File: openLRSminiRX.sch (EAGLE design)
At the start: 32 parts, among them IC1 MCP1703CB, U1 ATMEGA328P, Y1 16MHz

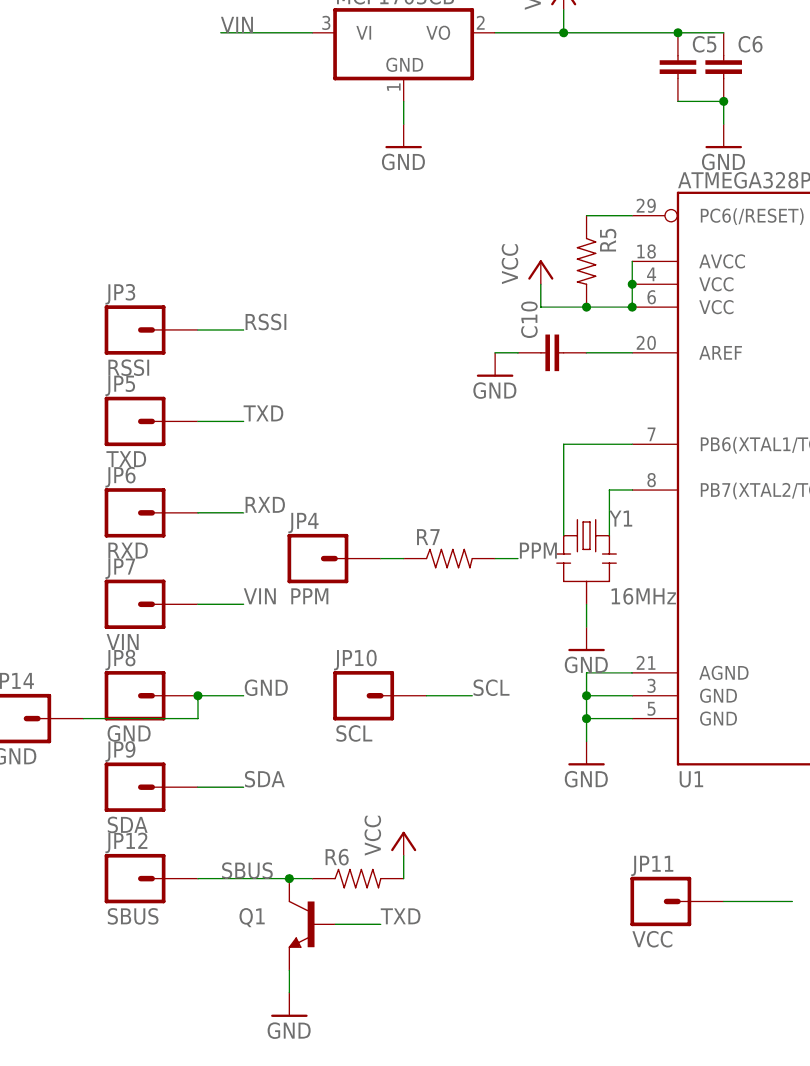
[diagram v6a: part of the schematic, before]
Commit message: Fix SBUS inverter (add resistor between TXD and NPN B) Add DTR breakout (easier serial flashing)
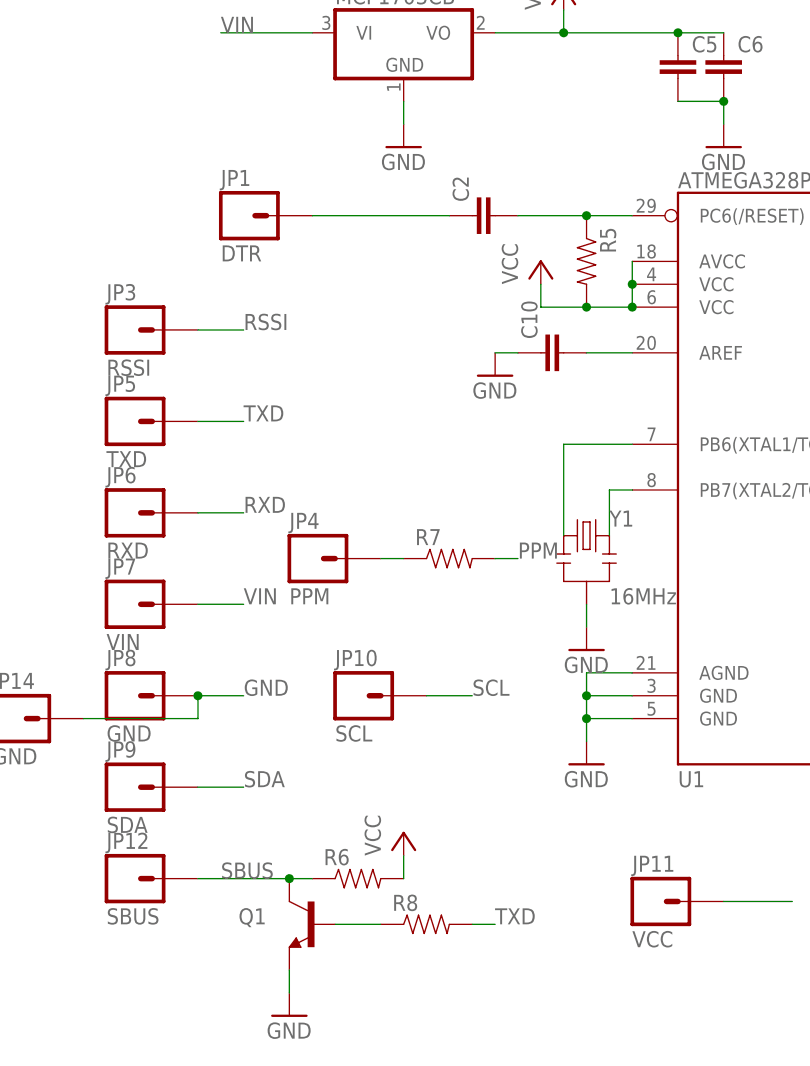
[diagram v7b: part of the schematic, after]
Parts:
- added C2: (no value), SparkFun-Capacitors:CAP0805
- added JP1: DTR, SparkFun-Connectors:M01PTH
- added R8: (no value), SparkFun-Resistors:RESISTOR0805-RES
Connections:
- new net N$20: C2.1, JP1.1
- new net N$21: Q1.B, R8.1
- net N$18: now also C2.2
- net TXD: now also R8.2; no longer Q1.B
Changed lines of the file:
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@@
 <?xml version="1.0" encoding="utf-8"?>
 <!DOCTYPE eagle SYSTEM "eagle.dtd">
-<eagle version="6.4">
+<eagle version="7.1.0">
 <drawing>
 <settings>
@@
 <part name="Y1" library="SparkFun-FreqCtrl" deviceset="RESONATOR" device="16MHZ" value="16MHz"/>
 <part name="GND12" library="supply1" deviceset="GND" device=""/>
+<part name="JP1" library="SparkFun-Connectors" deviceset="M01" device="PTH" value="DTR"/>
+<part name="C2" library="SparkFun-Capacitors" deviceset="CAP" device="0805"/>
+<part name="R8" library="SparkFun-Resistors" deviceset="RESISTOR" device="0805-RES"/>
 </parts>
 <sheets>
@@
 <instance part="Y1" gate="G$1" x="22.86" y="50.8"/>
 <instance part="GND12" gate="1" x="22.86" y="38.1"/>
+<instance part="JP1" gate="G$1" x="-15.24" y="86.36"/>
+<instance part="C2" gate="G$1" x="12.7" y="86.36" rot="R90"/>
+<instance part="R8" gate="G$1" x="5.08" y="7.62"/>
 </instances>
 <busses>
@@
 </segment>
 <segment>
-<pinref part="Q1" gate="G$1" pin="B"/>
-<wire x1="-5.08" y1="7.62" x2="0" y2="7.62" width="0.1524" layer="91"/>
-<label x="0" y="7.62" size="1.778" layer="95"/>
+<pinref part="R8" gate="G$1" pin="2"/>
+<wire x1="10.16" y1="7.62" x2="12.7" y2="7.62" width="0.1524" layer="91"/>
+<label x="12.7" y="7.62" size="1.778" layer="95"/>
 </segment>
 </net>
@@
 <pinref part="U1" gate="G$1" pin="PC6(/RESET)"/>
 <wire x1="22.86" y1="86.36" x2="27.94" y2="86.36" width="0.1524" layer="91"/>
+<pinref part="C2" gate="G$1" pin="2"/>
+<wire x1="22.86" y1="86.36" x2="15.24" y2="86.36" width="0.1524" layer="91"/>
+<junction x="22.86" y="86.36"/>
 </segment>
 </net>
@@
 </segment>
 </net>
+<net name="N$20" class="0">
+<segment>
+<pinref part="JP1" gate="G$1" pin="1"/>
+<pinref part="C2" gate="G$1" pin="1"/>
+<wire x1="-7.62" y1="86.36" x2="7.62" y2="86.36" width="0.1524" layer="91"/>
+</segment>
+</net>
+<net name="N$21" class="0">
+<segment>
+<pinref part="R8" gate="G$1" pin="1"/>
+<pinref part="Q1" gate="G$1" pin="B"/>
+<wire x1="0" y1="7.62" x2="-5.08" y2="7.62" width="0.1524" layer="91"/>
+</segment>
+</net>

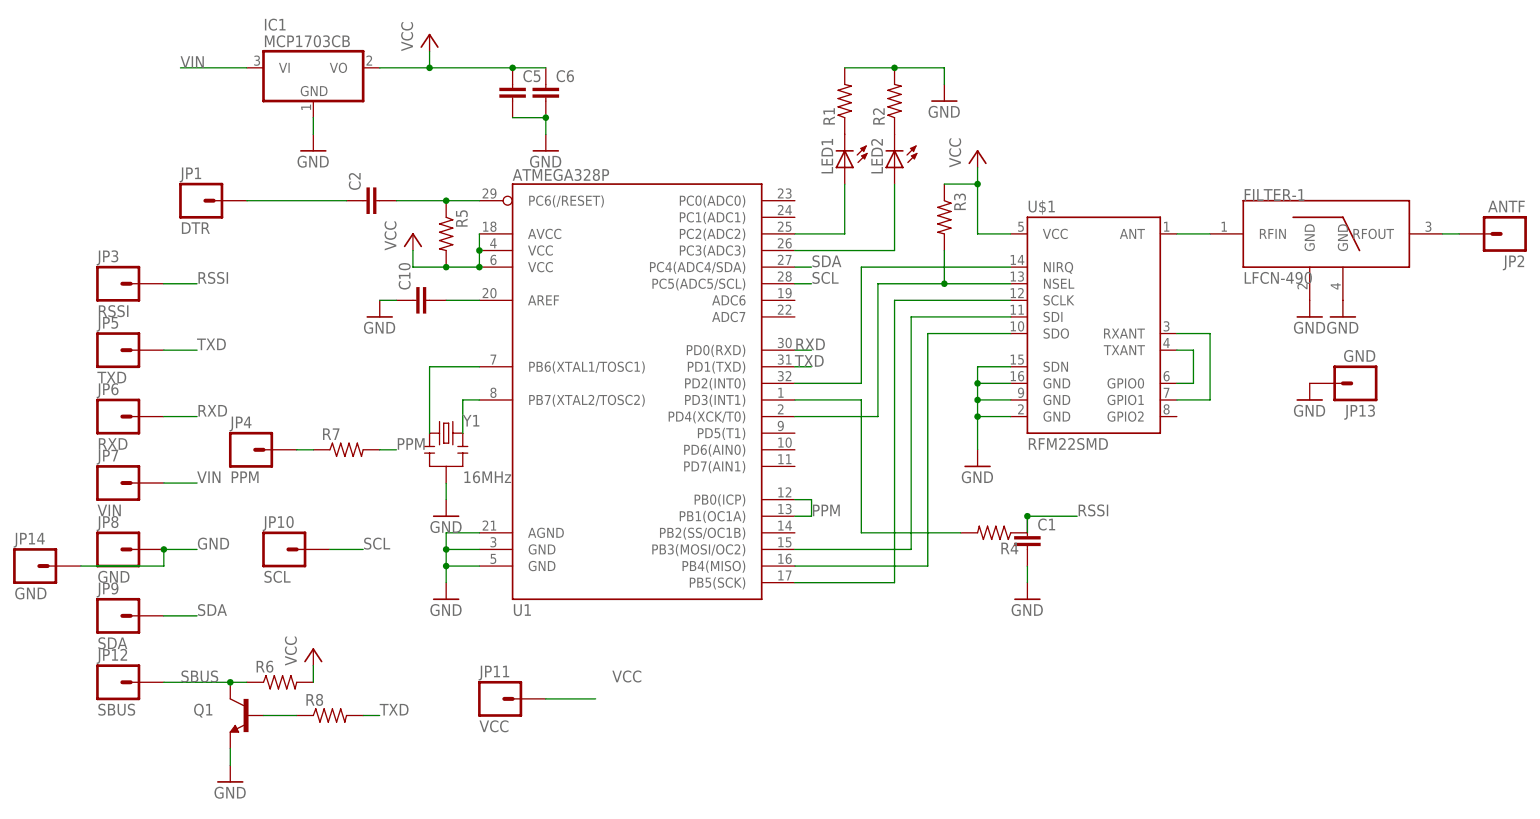
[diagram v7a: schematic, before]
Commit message: Add component values
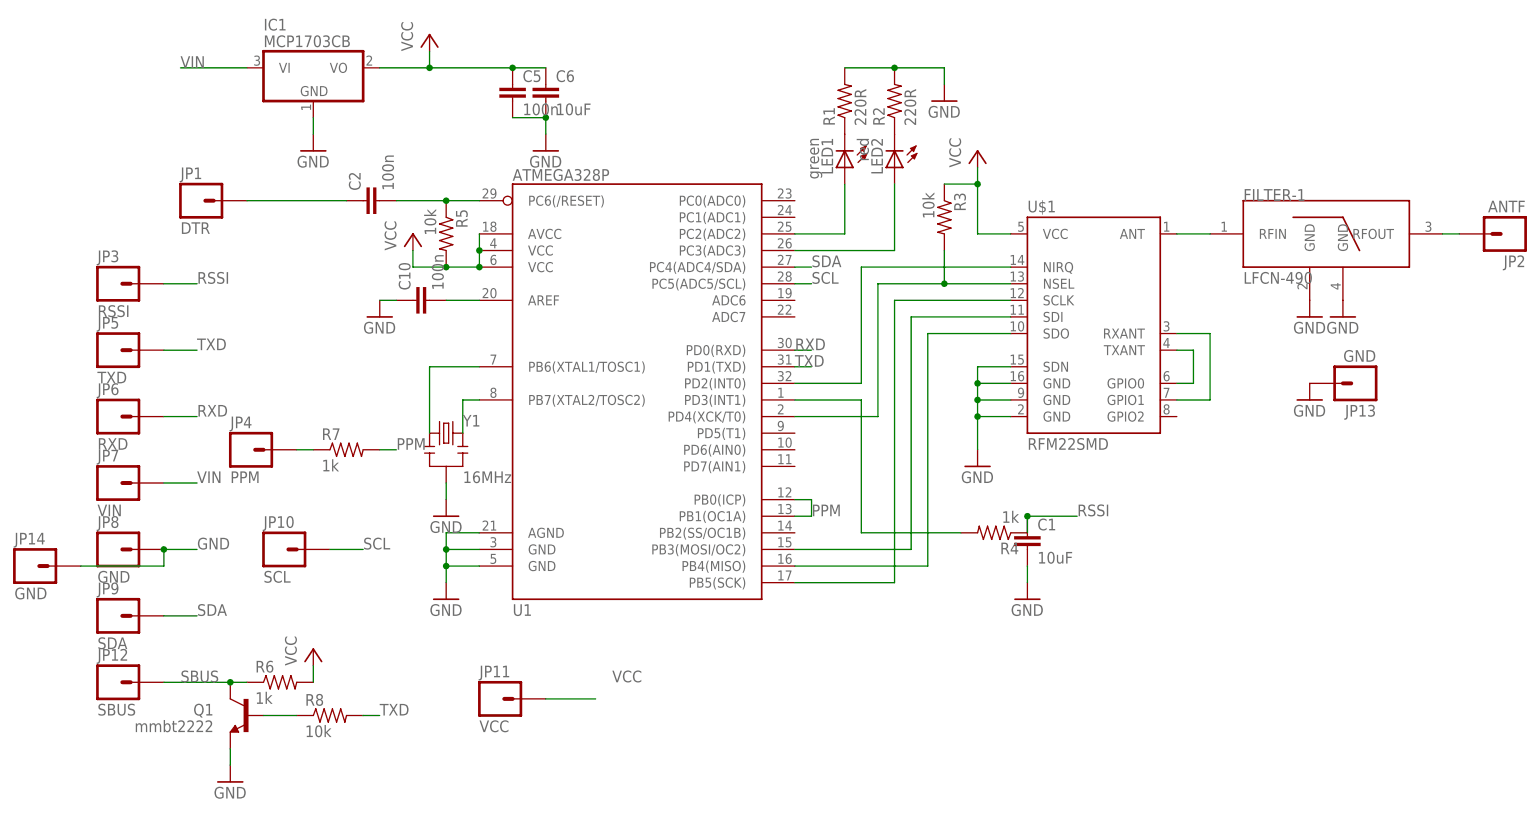
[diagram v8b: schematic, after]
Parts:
- C1, C6: value (none) -> 10uF
- C10, C2, C5: value (none) -> 100n
- LED1: value (none) -> green
- LED2: value (none) -> red
- Q1: value (none) -> mmbt2222
- R1, R2: value (none) -> 220R
- R3, R5, R8: value (none) -> 10k
- R4, R6, R7: value (none) -> 1k
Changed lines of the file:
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@@
 <?xml version="1.0" encoding="utf-8"?>
 <!DOCTYPE eagle SYSTEM "eagle.dtd">
-<eagle version="7.1.0">
+<eagle version="7.2.0">
 <drawing>
 <settings>
@@
 <part name="U$1" library="SparkFun-RF" deviceset="RFM22" device="SMD"/>
 <part name="U1" library="SparkFun-DigitalIC" deviceset="ATMEGA328_SMT" device="" value="ATMEGA328P"/>
-<part name="R1" library="SparkFun-Resistors" deviceset="RESISTOR" device="0805-RES"/>
+<part name="R1" library="SparkFun-Resistors" deviceset="RESISTOR" device="0805-RES" value="220R"/>
 <part name="GND1" library="supply1" deviceset="GND" device=""/>
 <part name="P+1" library="supply1" deviceset="VCC" device=""/>
 <part name="GND2" library="supply1" deviceset="GND" device=""/>
-<part name="LED1" library="led" deviceset="LED" device="SML0805"/>
-<part name="LED2" library="led" deviceset="LED" device="SML0805"/>
-<part name="R2" library="SparkFun-Resistors" deviceset="RESISTOR" device="0805-RES"/>
+<part name="LED1" library="led" deviceset="LED" device="SML0805" value="green"/>
+<part name="LED2" library="led" deviceset="LED" device="SML0805" value="red"/>
+<part name="R2" library="SparkFun-Resistors" deviceset="RESISTOR" device="0805-RES" value="220R"/>
 <part name="P+2" library="supply1" deviceset="VCC" device=""/>
 <part name="GND4" library="supply1" deviceset="GND" device=""/>
-<part name="R4" library="SparkFun-Resistors" deviceset="RESISTOR" device="0805-RES"/>
+<part name="R4" library="SparkFun-Resistors" deviceset="RESISTOR" device="0805-RES" value="1k"/>
 <part name="GND6" library="supply1" deviceset="GND" device=""/>
-<part name="C5" library="SparkFun-Capacitors" deviceset="CAP" device="0805"/>
-<part name="C6" library="SparkFun-Capacitors" deviceset="CAP" device="0805"/>
+<part name="C5" library="SparkFun-Capacitors" deviceset="CAP" device="0805" value="100n"/>
+<part name="C6" library="SparkFun-Capacitors" deviceset="CAP" device="0805" value="10uF"/>
 <part name="GND7" library="supply1" deviceset="GND" device=""/>
-<part name="R5" library="SparkFun-Resistors" deviceset="RESISTOR" device="0805-RES"/>
+<part name="R5" library="SparkFun-Resistors" deviceset="RESISTOR" device="0805-RES" value="10k"/>
 <part name="P+3" library="supply1" deviceset="VCC" device=""/>
-<part name="C10" library="SparkFun-Capacitors" deviceset="CAP" device="0805"/>
+<part name="C10" library="SparkFun-Capacitors" deviceset="CAP" device="0805" value="100n"/>
 <part name="GND8" library="supply1" deviceset="GND" device=""/>
-<part name="Q1" library="SparkFun-DiscreteSemi" deviceset="TRANSISTOR_NPN" device="SOT23"/>
-<part name="R6" library="SparkFun-Resistors" deviceset="RESISTOR" device="0805-RES"/>
+<part name="Q1" library="SparkFun-DiscreteSemi" deviceset="TRANSISTOR_NPN" device="SOT23" value="mmbt2222"/>
+<part name="R6" library="SparkFun-Resistors" deviceset="RESISTOR" device="0805-RES" value="1k"/>
 <part name="GND3" library="supply1" deviceset="GND" device=""/>
 <part name="P+4" library="supply1" deviceset="VCC" device=""/>
-<part name="C1" library="SparkFun-Capacitors" deviceset="CAP" device="0805"/>
+<part name="C1" library="SparkFun-Capacitors" deviceset="CAP" device="0805" value="10uF"/>
 <part name="GND5" library="supply1" deviceset="GND" device=""/>
 <part name="FILTER-1" library="minicircuits" deviceset="LFCN" device="-490"/>
@@
 <part name="JP14" library="SparkFun-Connectors" deviceset="M01" device="PTH" value="GND"/>
 <part name="GND11" library="supply1" deviceset="GND" device=""/>
-<part name="R3" library="SparkFun-Resistors" deviceset="RESISTOR" device="0805-RES"/>
-<part name="R7" library="SparkFun-Resistors" deviceset="RESISTOR" device="0805-RES"/>
+<part name="R3" library="SparkFun-Resistors" deviceset="RESISTOR" device="0805-RES" value="10k"/>
+<part name="R7" library="SparkFun-Resistors" deviceset="RESISTOR" device="0805-RES" value="1k"/>
 <part name="Y1" library="SparkFun-FreqCtrl" deviceset="RESONATOR" device="16MHZ" value="16MHz"/>
 <part name="GND12" library="supply1" deviceset="GND" device=""/>
 <part name="JP1" library="SparkFun-Connectors" deviceset="M01" device="PTH" value="DTR"/>
-<part name="C2" library="SparkFun-Capacitors" deviceset="CAP" device="0805"/>
-<part name="R8" library="SparkFun-Resistors" deviceset="RESISTOR" device="0805-RES"/>
+<part name="C2" library="SparkFun-Capacitors" deviceset="CAP" device="0805" value="100n"/>
+<part name="R8" library="SparkFun-Resistors" deviceset="RESISTOR" device="0805-RES" value="10k"/>
 </parts>
 <sheets>
